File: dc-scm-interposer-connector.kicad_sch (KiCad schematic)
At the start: 2 parts, among them J2001 PinSocket_2x10_P2.54mm_SMD, J2002 PinSocket_2x10_P2.54mm_SMD

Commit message: chore: set date and project name
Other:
- company: (none) -> Antmicro
- title: (none) -> eSPI Adapter
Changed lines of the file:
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@@
 	(generator_version "10.0")
 	(paper "A4")
+	(title_block
+		(title "eSPI Adapter")
+		(date "2026-08-21")
+		(rev "1.0.0")
+		(company "Antmicro")
+	)
 	(text "DC-SCM Interposer Connectors"
 		(exclude_from_sim no)

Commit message: [#103224] Initial placement/visualization
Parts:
- removed J2001, J2002: PinSocket_2x10_P2.54mm_SMD, antmicro-footprints:PinSocket_2x10_P2.54mm_SMD, symbol Antmicro Symbols:PinSocket_2x10_P2.54mm_SMD
- added J2003: PinSocket_2x8_P2.54mm_SMD, antmicro-footprints:PinSocket_2x8_P2.54mm_SMD, symbol Antmicro Symbols:PinSocket_2x8_P2.54mm_SMD
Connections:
- net DC_SCM_12V_AUX: now also J2003.16
- net DC_SCM_P3V0: now also J2003.14
- net DC_SCM_STBY_EN: now also J2003.15
- net EC_ESPI.IO0: now also J2003.8
- net EC_ESPI.IO1: now also J2003.1
- net EC_ESPI.IO2: now also J2003.3
- net EC_ESPI.IO3: now also J2003.5
- net EC_ESPI.SCK: now also J2003.2
- net EC_ESPI.~{ALERT0}: now also J2003.7
- net EC_ESPI.~{CS0}: now also J2003.4
- net EC_ESPI.~{RESET}: now also J2003.6
- net GND: now also J2003.10, J2003.12, J2003.9
- no-connect marks 6 -> 2
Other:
- note added: "DC-SCM Interposer Connector"
- note removed: "DC-SCM Interposer Connectors"
- note removed: "Not connected to anything Used only for mechanical purposes!"
- note removed: "TODO: Decide how many additional, disconnected connectors are needed for mechanical stability"

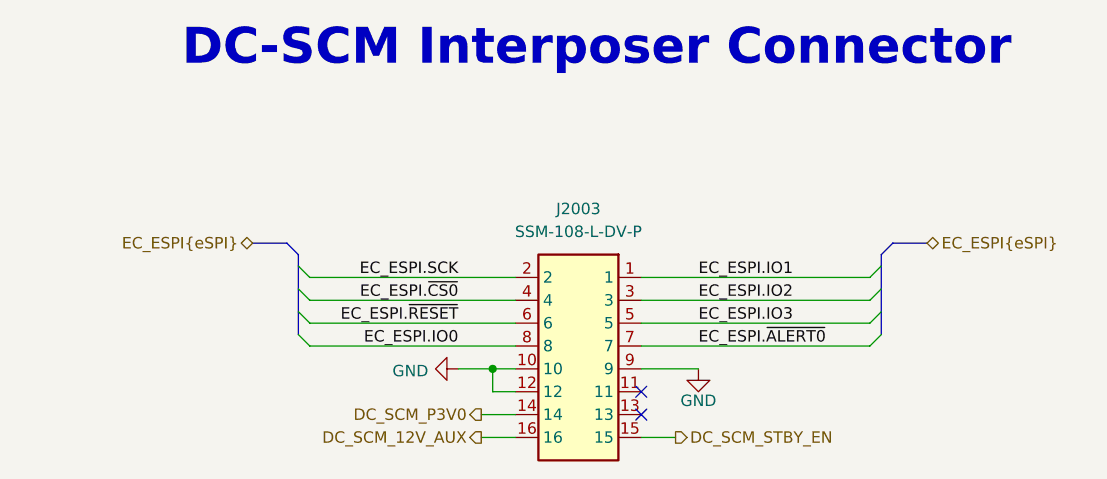
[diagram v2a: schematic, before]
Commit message: [#103697] Change key sectors placement (DC-DC, 7seg, Flash, FTDI), Change buttons, Change DC-SCM connector to angled header
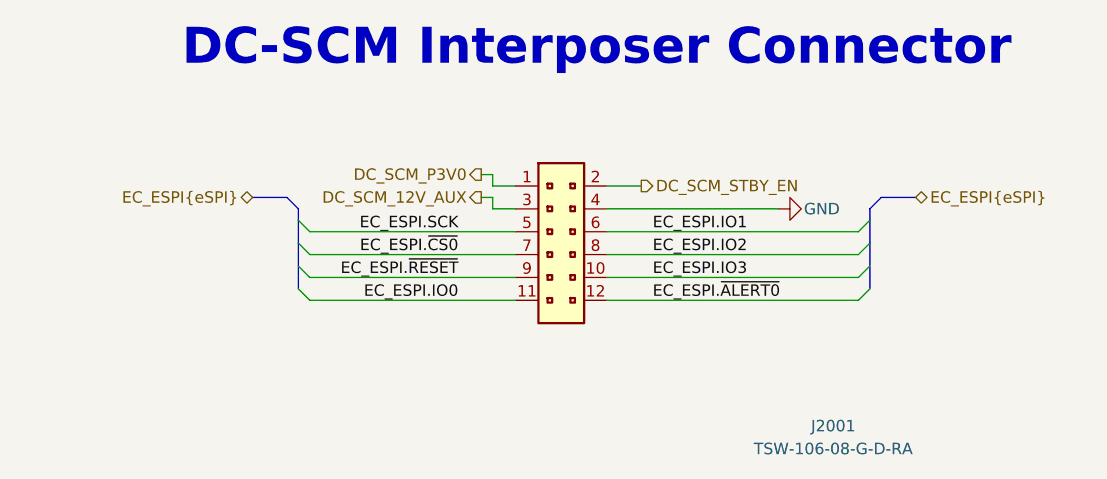
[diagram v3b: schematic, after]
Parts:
- removed J2003: PinSocket_2x8_P2.54mm_SMD, antmicro-footprints:PinSocket_2x8_P2.54mm_SMD, symbol Antmicro Symbols:PinSocket_2x8_P2.54mm_SMD
- added J2001: PinHeader_2x6_P2.54mm_Drill1.1mm_Horizontal, antmicro-footprints:PinHeader_2x6_P2.54mm_Drill1.1mm_Horizontal_ALT, symbol Antmicro Symbols:PinHeader_2x6_P2.54mm_Drill1.1mm_Horizontal_TSW-106-08-G-D-RA
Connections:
- net DC_SCM_12V_AUX: now also J2001.3
- net DC_SCM_P3V0: now also J2001.1
- net DC_SCM_STBY_EN: now also J2001.2
- net EC_ESPI.IO0: now also J2001.11
- net EC_ESPI.IO1: now also J2001.6
- net EC_ESPI.IO2: now also J2001.8
- net EC_ESPI.IO3: now also J2001.10
- net EC_ESPI.SCK: now also J2001.5
- net EC_ESPI.~{ALERT0}: now also J2001.12
- net EC_ESPI.~{CS0}: now also J2001.7
- net EC_ESPI.~{RESET}: now also J2001.9
- net GND: now also J2001.4
- no-connect marks 2 -> 0

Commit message: [#103811] Replace FT232RL with FT2232H - unifinished
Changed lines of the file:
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@@
 		(dnp no)
 		(property "Reference" "J2001"
-			(at 180.086 113.03 0)
+			(at 149.606 78.74 0)
 			(show_name no)
 			(do_not_autoplace no)
@@
 		)
 		(property "MPN" "TSW-106-08-G-D-RA"
-			(at 180.086 115.57 0)
+			(at 149.606 81.28 0)
 			(show_name no)
 			(do_not_autoplace no)

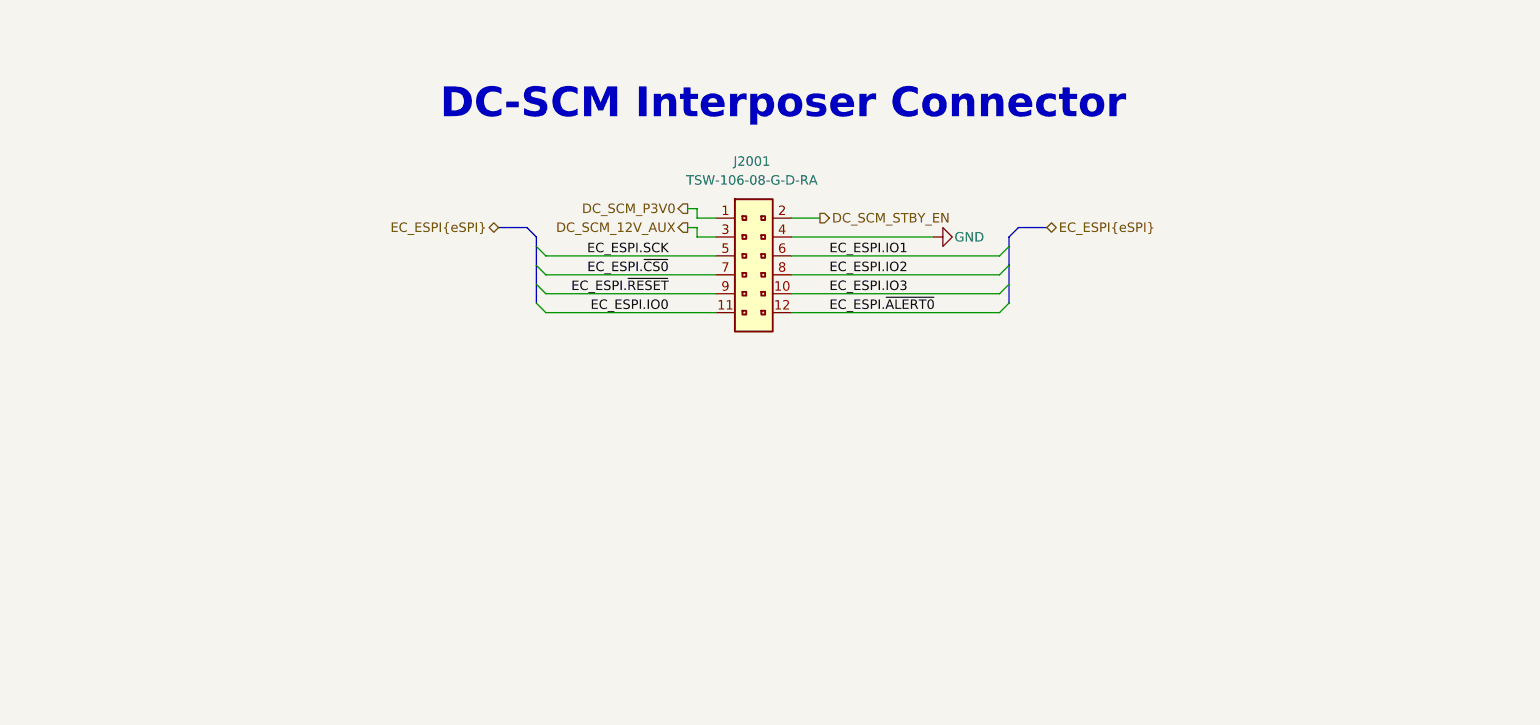
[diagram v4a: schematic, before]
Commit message: [#103753] Fix issues according to the review, add FT2232 to the schematic
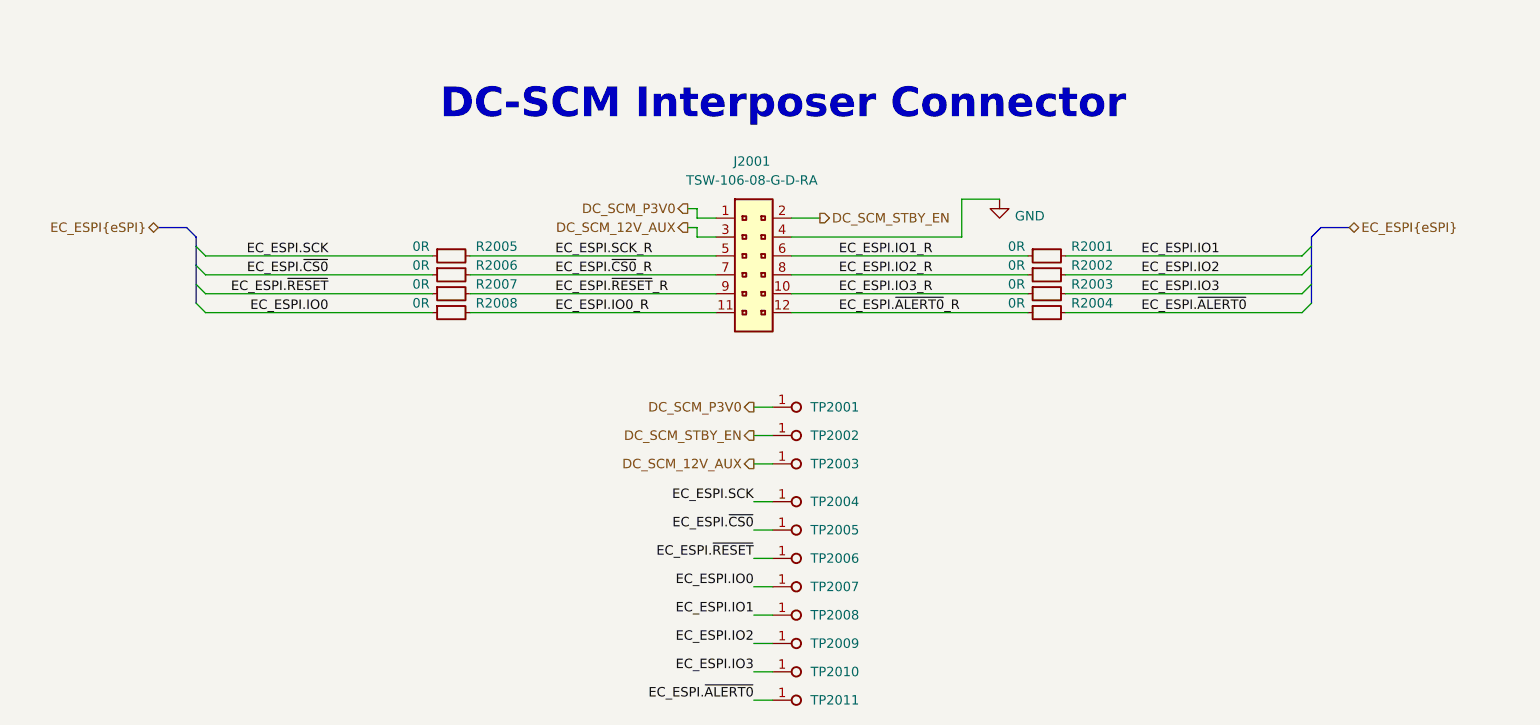
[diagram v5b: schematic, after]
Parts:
- added R2001, R2002, R2003, R2004, R2005, R2006, R2007, R2008: R_0R_0402, antmicro-footprints:R_0402_1005Metric, symbol Antmicro Symbols:R_0R_0402
- added TP2001, TP2002, TP2003, TP2004, TP2005, TP2006, TP2007, TP2008, TP2009, TP2010, TP2011: TP_1mm_SMD, antmicro-footprints:TP_SMD_1mm, symbol antmicroTestPoints:TP_1mm_SMD
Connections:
- net DC_SCM_12V_AUX: now also TP2003.1
- net DC_SCM_P3V0: now also TP2001.1
- net DC_SCM_STBY_EN: now also TP2002.1
- net EC_ESPI.IO0: now also R2008.1, TP2007.1; no longer J2001.11
- net EC_ESPI.IO1: now also R2001.2, TP2008.1; no longer J2001.6
- net EC_ESPI.IO2: now also R2002.2, TP2009.1; no longer J2001.8
- net EC_ESPI.IO3: now also R2003.2, TP2010.1; no longer J2001.10
- net EC_ESPI.SCK: now also R2005.1, TP2004.1; no longer J2001.5
- net EC_ESPI.~{ALERT0}: now also R2004.2, TP2011.1; no longer J2001.12
- net EC_ESPI.~{CS0}: now also R2006.1, TP2005.1; no longer J2001.7
- net EC_ESPI.~{RESET}: now also R2007.1, TP2006.1; no longer J2001.9
- new net EC_ESPI.IO0_R: J2001.11, R2008.2
- new net EC_ESPI.IO1_R: J2001.6, R2001.1
- new net EC_ESPI.IO2_R: J2001.8, R2002.1
- new net EC_ESPI.IO3_R: J2001.10, R2003.1
- new net EC_ESPI.SCK_R: J2001.5, R2005.2
- new net EC_ESPI.~{ALERT0}_R: J2001.12, R2004.1
- new net EC_ESPI.~{CS0}_R: J2001.7, R2006.2
- new net EC_ESPI.~{RESET}_R: J2001.9, R2007.2

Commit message: [#103696] Implementing changes from review onto PCB
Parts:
- removed TP2001: TP_1mm_SMD, antmicro-footprints:TP_SMD_1mm, symbol antmicroTestPoints:TP_1mm_SMD
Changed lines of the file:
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@@
-	(wire
-		(pts
-			(xy 149.86 111.76) (xy 152.4 111.76)
-		)
-		(stroke
-			(width 0)
-			(type default)
-		)
-	)
 	(wire
 		(pts
@@
 			)
 			(justify right bottom)
-		)
-	)
-	(hierarchical_label "DC_SCM_P3V0"
-		(shape output)
-		(at 149.86 111.76 180)
-		(effects
-			(font
-				(size 1.27 1.27)
-			)
-			(justify right)
 		)
 	)
@@
 					(unit 1)
 				)
-			)
-		)
-	)
-	(symbol
-		(lib_id "antmicroTestPoints:TP_1mm_SMD")
-		(at 152.4 111.76 0)
-		(unit 1)
-		(body_style 1)
-		(exclude_from_sim no)
-		(in_bom no)
-		(on_board yes)
-		(in_pos_files yes)
-		(dnp no)
-		(fields_autoplaced yes)
-		(property "Reference" "TP2001"
-			(at 157.48 111.76 0)
-			(show_name no)
-			(do_not_autoplace no)
-			(effects
-				(font
-					(size 1.27 1.27)
-					(thickness 0.15)
-				)
-				(justify left)
-			)
-		)
-		(property "Value" "TP_1mm_SMD"
-			(at 167.64 119.38 0)
-			(hide yes)
-			(show_name no)
-			(do_not_autoplace no)
-			(effects
-				(font
-					(size 1.27 1.27)
-					(thickness 0.15)
-				)
-				(justify left bottom)
-			)
-		)
-		(property "Footprint" "antmicro-footprints:TP_SMD_1mm"
-			(at 167.64 121.92 0)
-			(hide yes)
-			(show_name no)
-			(do_not_autoplace no)
-			(effects
-				(font
-					(size 1.27 1.27)
-					(thickness 0.15)
-				)
-				(justify left bottom)
-			)
-		)
-		(property "Datasheet" ""
-			(at 170.18 124.46 0)
-			(hide yes)
-			(show_name no)
-			(do_not_autoplace no)
-			(effects
-				(font
-					(size 1.27 1.27)
-					(thickness 0.15)
-				)
-				(justify left bottom)
-			)
-		)
-		(property "Description" "Test point 1mm SMD"
-			(at 167.64 132.08 0)
-			(hide yes)
-			(show_name no)
-			(do_not_autoplace no)
-			(effects
-				(font
-					(size 1.27 1.27)
-				)
-				(justify left bottom)
-			)
-		)
-		(property "MPN" ""
-			(at 152.4 111.76 0)
-			(hide yes)
-			(show_name no)
-			(do_not_autoplace no)
-			(effects
-				(font
-					(size 1.27 1.27)
-				)
-			)
-		)
-		(property "Manufacturer" ""
-			(at 152.4 111.76 0)
-			(hide yes)
-			(show_name no)
-			(do_not_autoplace no)
-			(effects
-				(font
-					(size 1.27 1.27)
-				)
-			)
-		)
-		(property "Author" "Antmicro"
-			(at 167.64 127 0)
-			(hide yes)
-			(show_name no)
-			(do_not_autoplace no)
-			(effects
-				(font
-					(size 1.27 1.27)
-					(thickness 0.15)
-				)
-				(justify left bottom)
-			)
-		)
-		(property "License" "Apache-2.0"
-			(at 167.64 129.54 0)
-			(hide yes)
-			(show_name no)
-			(do_not_autoplace no)
-			(effects
-				(font
-					(size 1.27 1.27)
-					(thickness 0.15)
-				)
-				(justify left bottom)
-			)
-		)
-		(pin "1"
-		)
-		(instances
-			(project "dc-scm-server-integration-espi-adapter"
-				(path "/df391740-647e-4ab6-9dcd-d61184d66fe9/dad11b40-64da-40df-af81-feff62248020"
-					(reference "TP2001")
-					(unit 1)
-				)

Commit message: [#103753] Update symbol libraries
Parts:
- J2001: symbol Antmicro Symbols:PinHeader_2x6_P2.54mm_Drill1.1mm_Horizontal_TSW-106-08-G-D-RA -> antmicroGenericPinHeaders:PinHeader_2x6_P2.54mm_Drill1.1mm_Horizontal_TSW-106-08-G-D-RA
- R2001, R2002, R2003, R2004, R2005, R2006, R2007, R2008: symbol Antmicro Symbols:R_0R_0402 -> antmicroResistors0402:R_0R_0402

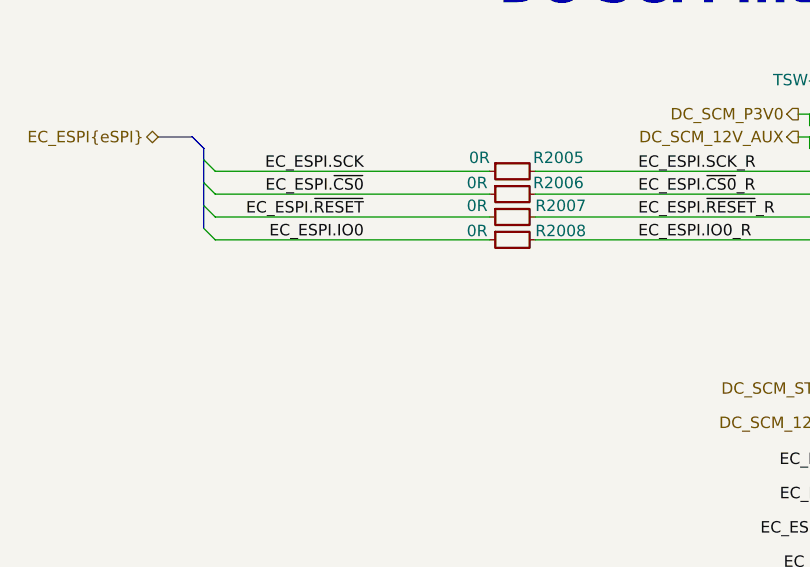
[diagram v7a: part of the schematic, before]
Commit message: [#103697] Change redundant LED connections, start PCB layout
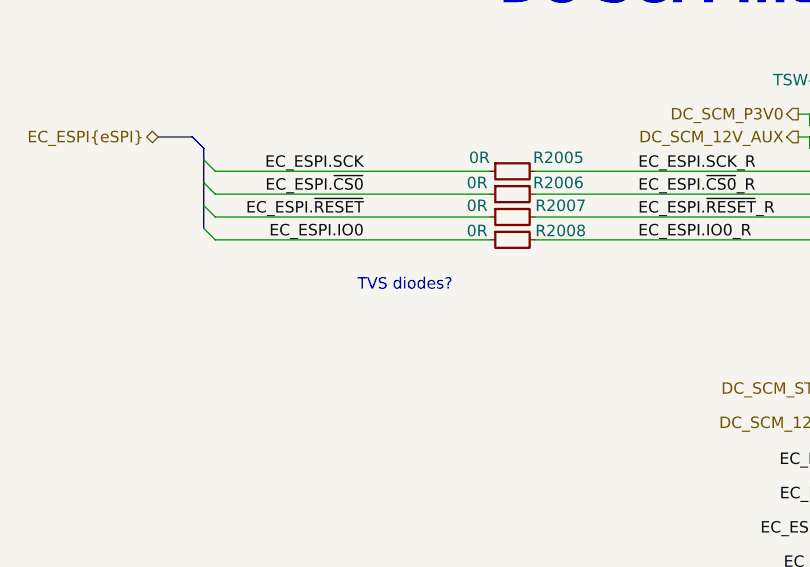
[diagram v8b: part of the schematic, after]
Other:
- note added: "TVS diodes?"
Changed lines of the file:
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@@
+		)
+	)
+	(text "TVS diodes?"
+		(exclude_from_sim no)
+		(at 97.282 104.14 0)
+		(effects
+			(font
+				(size 1.27 1.27)
+			)
 		)
 	)
@@
 		)
 	)
+	(label "EC_ESPI.IO1_R"
+		(at 161.29 91.44 0)
+		(effects
+			(font
+				(size 1.27 1.27)
+			)
+			(justify left bottom)
+		)
+	)
 	(label "EC_ESPI.~{RESET}_R"
 		(at 123.19 96.52 0)
@@
 		)
 	)
+	(label "EC_ESPI.~{RESET}"
+		(at 92.71 96.52 180)
+		(effects
+			(font
+				(size 1.27 1.27)
+			)
+			(justify right bottom)
+		)
+	)
+	(label "EC_ESPI.~{ALERT0}_R"
+		(at 161.29 99.06 0)
+		(effects
+			(font
+				(size 1.27 1.27)
+			)
+			(justify left bottom)
+		)
+	)
+	(label "EC_ESPI.IO2"
+		(at 201.93 93.98 0)
+		(effects
+			(font
+				(size 1.27 1.27)
+			)
+			(justify left bottom)
+		)
+	)
+	(label "EC_ESPI.~{CS0}"
+		(at 92.71 93.98 180)
+		(effects
+			(font
+				(size 1.27 1.27)
+			)
+			(justify right bottom)
+		)
+	)
+	(label "EC_ESPI.IO1"
+		(at 201.93 91.44 0)
+		(effects
+			(font
+				(size 1.27 1.27)
+			)
+			(justify left bottom)
+		)
+	)
+	(label "EC_ESPI.IO2"
+		(at 149.86 143.51 180)
+		(effects
+			(font
+				(size 1.27 1.27)
+			)
+			(justify right bottom)
+		)
+	)
+	(label "EC_ESPI.~{CS0}"
+		(at 149.86 128.27 180)
+		(effects
+			(font
+				(size 1.27 1.27)
+			)
+			(justify right bottom)
+		)
+	)
+	(label "EC_ESPI.~{ALERT0}"
+		(at 149.86 151.13 180)
+		(effects
+			(font
+				(size 1.27 1.27)
+			)
+			(justify right bottom)
+		)
+	)
+	(label "EC_ESPI.~{ALERT0}"
+		(at 201.93 99.06 0)
+		(effects
+			(font
+				(size 1.27 1.27)
+			)
+			(justify left bottom)
+		)
+	)
+	(label "EC_ESPI.IO0"
+		(at 92.71 99.06 180)
+		(effects
+			(font
+				(size 1.27 1.27)
+			)
+			(justify right bottom)
+		)
+	)
+	(label "EC_ESPI.SCK_R"
+		(at 123.19 91.44 0)
+		(effects
+			(font
+				(size 1.27 1.27)
+			)
+			(justify left bottom)
+		)
+	)
+	(label "EC_ESPI.IO1"
+		(at 149.86 139.7 180)
+		(effects
+			(font
+				(size 1.27 1.27)
+			)
+			(justify right bottom)
+		)
+	)
+	(label "EC_ESPI.~{CS0}_R"
+		(at 123.19 93.98 0)
+		(effects
+			(font
+				(size 1.27 1.27)
+			)
+			(justify left bottom)
+		)
+	)
+	(label "EC_ESPI.~{RESET}"
+		(at 149.86 132.08 180)
+		(effects
+			(font
+				(size 1.27 1.27)
+			)
+			(justify right bottom)
+		)
+	)
+	(label "EC_ESPI.IO0"
+		(at 149.86 135.89 180)
+		(effects
+			(font
+				(size 1.27 1.27)
+			)
+			(justify right bottom)
+		)
+	)
+	(label "EC_ESPI.IO3"
+		(at 149.86 147.32 180)
+		(effects
+			(font
+				(size 1.27 1.27)
+			)
+			(justify right bottom)
+		)
+	)
+	(label "EC_ESPI.IO2_R"
+		(at 161.29 93.98 0)
+		(effects
+			(font
+				(size 1.27 1.27)
+			)
+			(justify left bottom)
+		)
+	)
+	(label "EC_ESPI.IO3_R"
+		(at 161.29 96.52 0)
+		(effects
+			(font
+				(size 1.27 1.27)
+			)
+			(justify left bottom)
+		)
+	)
+	(label "EC_ESPI.SCK"
+		(at 92.71 91.44 180)
+		(effects
+			(font
+				(size 1.27 1.27)
+			)
+			(justify right bottom)
+		)
+	)
 	(label "EC_ESPI.IO3"
 		(at 201.93 96.52 0)
@@
 		)
 	)
-	(label "EC_ESPI.~{RESET}"
-		(at 92.71 96.52 180)
-		(effects
-			(font
-				(size 1.27 1.27)
-			)
-			(justify right bottom)
-		)
-	)
-	(label "EC_ESPI.~{ALERT0}_R"
-		(at 161.29 99.06 0)
-		(effects
-			(font
-				(size 1.27 1.27)
-			)
-			(justify left bottom)
-		)
-	)
-	(label "EC_ESPI.IO2"
-		(at 201.93 93.98 0)
-		(effects
-			(font
-				(size 1.27 1.27)
-			)
-			(justify left bottom)
-		)
-	)
-	(label "EC_ESPI.~{CS0}"
-		(at 92.71 93.98 180)
-		(effects
-			(font
-				(size 1.27 1.27)
-			)
-			(justify right bottom)
-		)
-	)
-	(label "EC_ESPI.IO1_R"
-		(at 161.29 91.44 0)
-		(effects
-			(font
-				(size 1.27 1.27)
-			)
-			(justify left bottom)
-		)
-	)
-	(label "EC_ESPI.IO3_R"
-		(at 161.29 96.52 0)
-		(effects
-			(font
-				(size 1.27 1.27)
-			)
-			(justify left bottom)
-		)
-	)
-	(label "EC_ESPI.IO2"
-		(at 149.86 143.51 180)
-		(effects
-			(font
-				(size 1.27 1.27)
-			)
-			(justify right bottom)
-		)
-	)
-	(label "EC_ESPI.~{CS0}"
-		(at 149.86 128.27 180)
-		(effects
-			(font
-				(size 1.27 1.27)
-			)
-			(justify right bottom)
-		)
-	)
-	(label "EC_ESPI.~{ALERT0}"
-		(at 149.86 151.13 180)
-		(effects
-			(font
-				(size 1.27 1.27)
-			)
-			(justify right bottom)
-		)
-	)
-	(label "EC_ESPI.~{ALERT0}"
-		(at 201.93 99.06 0)
-		(effects
-			(font
-				(size 1.27 1.27)
-			)
-			(justify left bottom)
-		)
-	)
-	(label "EC_ESPI.IO0"
-		(at 92.71 99.06 180)
-		(effects
-			(font
-				(size 1.27 1.27)
-			)
-			(justify right bottom)
-		)
-	)
-	(label "EC_ESPI.SCK_R"
-		(at 123.19 91.44 0)
-		(effects
-			(font
-				(size 1.27 1.27)
-			)
-			(justify left bottom)
-		)
-	)
-	(label "EC_ESPI.IO1"
-		(at 149.86 139.7 180)
-		(effects
-			(font
-				(size 1.27 1.27)
-			)
-			(justify right bottom)
-		)
-	)
-	(label "EC_ESPI.~{CS0}_R"
-		(at 123.19 93.98 0)
-		(effects
-			(font
-				(size 1.27 1.27)
-			)
-			(justify left bottom)
-		)
-	)
-	(label "EC_ESPI.~{RESET}"
-		(at 149.86 132.08 180)
-		(effects
-			(font
-				(size 1.27 1.27)
-			)
-			(justify right bottom)
-		)
-	)
-	(label "EC_ESPI.IO0"
-		(at 149.86 135.89 180)
-		(effects
-			(font
-				(size 1.27 1.27)
-			)
-			(justify right bottom)
-		)
-	)
-	(label "EC_ESPI.IO3"
-		(at 149.86 147.32 180)
-		(effects
-			(font
-				(size 1.27 1.27)
-			)
-			(justify right bottom)
-		)
-	)
-	(label "EC_ESPI.IO1"
-		(at 201.93 91.44 0)
-		(effects
-			(font
-				(size 1.27 1.27)
-			)
-			(justify left bottom)
-		)
-	)
-	(label "EC_ESPI.IO2_R"
-		(at 161.29 93.98 0)
-		(effects
-			(font
-				(size 1.27 1.27)
-			)
-			(justify left bottom)
-		)
-	)
-	(label "EC_ESPI.SCK"
-		(at 92.71 91.44 180)
-		(effects
-			(font
-				(size 1.27 1.27)
-			)
-			(justify right bottom)
-		)
-	)
